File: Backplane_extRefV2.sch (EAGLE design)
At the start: 13 parts, among them J1 TFM-125-02-XXX-D-WT, U1 TLE2426CD

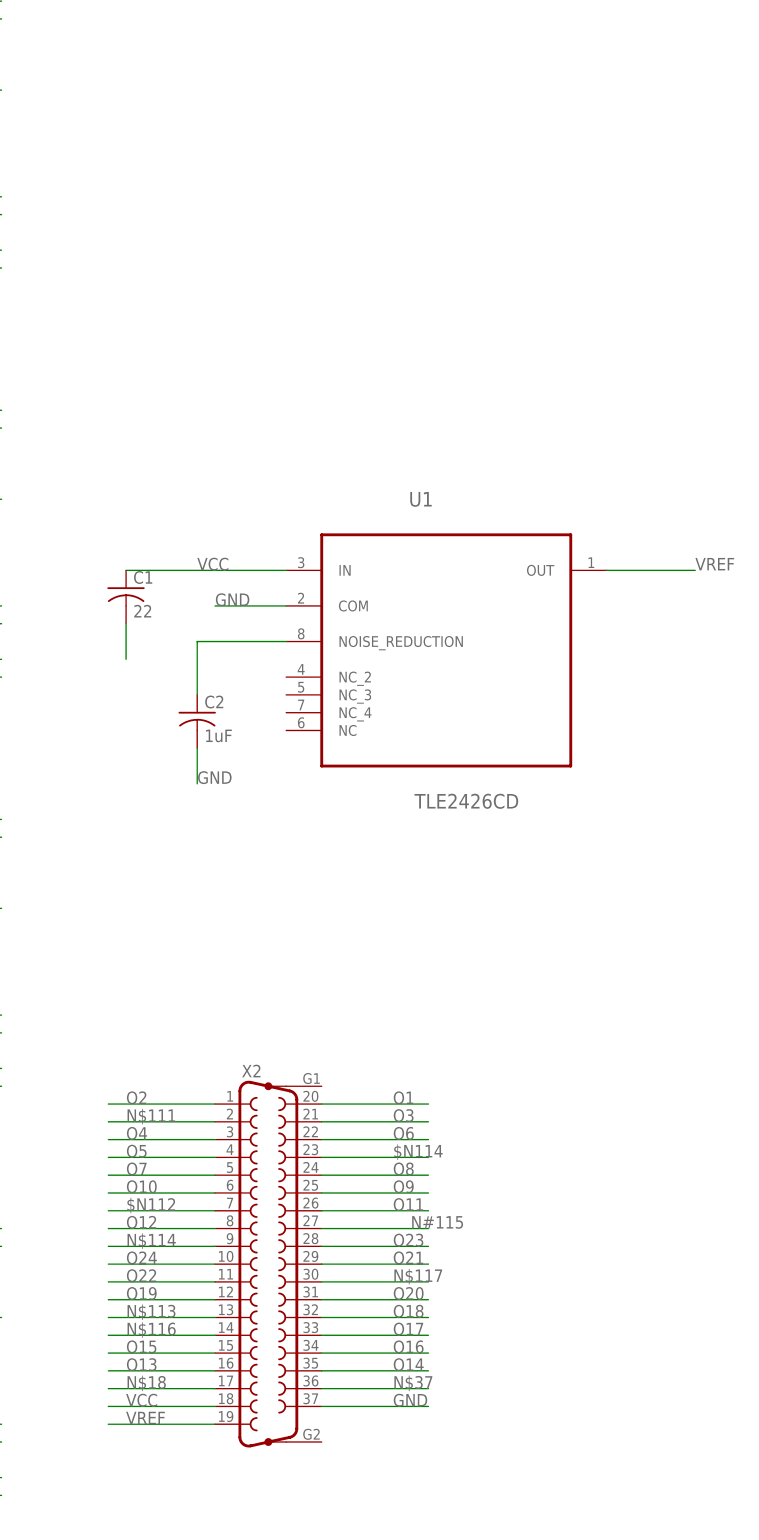
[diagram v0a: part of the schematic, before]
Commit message: minor updates to routing. Added DC-DC voltage converter/isolator to backplaneV2 & 24ch brd
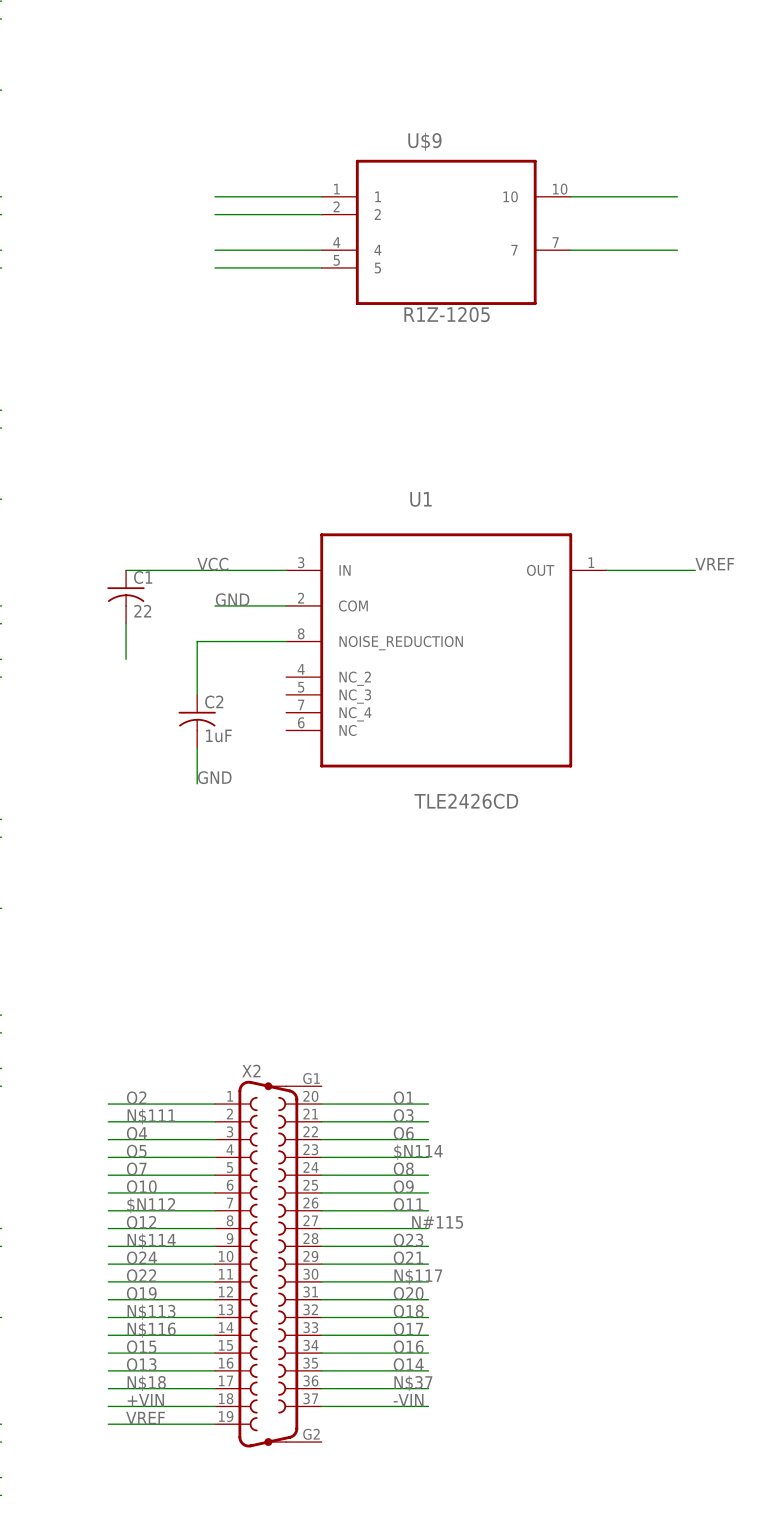
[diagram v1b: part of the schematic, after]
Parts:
- added U$9: R1Z-1205, tuckerLib:R1Z-1205
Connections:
- new net +VIN: U$9.2, X2.18
- new net -VIN: U$9.1, X2.37
- new net NC2: U$9.10
- net GND: now also U$9.4, U$9.5; no longer X2.37
- net VCC: now also U$9.7; no longer X2.18
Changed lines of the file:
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@@
 <part name="U$7" library="SAMTEC-FLE-Mxx-Sxx_By_element14_Batch_1" deviceset="FLE-116-01-G-DV" device=""/>
 <part name="U$8" library="SAMTEC-FLE-Mxx-Sxx_By_element14_Batch_1" deviceset="FLE-116-01-G-DV" device=""/>
+<part name="U$9" library="tuckerLib" deviceset="R1Z-1205" device=""/>
 </parts>
 <sheets>
@@
 <instance part="U$7" gate="A" x="66.04" y="-33.02"/>
 <instance part="U$8" gate="A" x="66.04" y="-93.98"/>
+<instance part="U$9" gate="G$1" x="162.56" y="182.88"/>
 </instances>
 <busses>
@@
 </segment>
 <segment>
-<pinref part="X2" gate="G$1" pin="37"/>
-<wire x1="144.78" y1="15.24" x2="160.02" y2="15.24" width="0.1524" layer="91"/>
-<label x="154.94" y="15.24" size="1.778" layer="95"/>
+<pinref part="U$9" gate="G$1" pin="4"/>
+<wire x1="144.78" y1="180.34" x2="129.54" y2="180.34" width="0.1524" layer="91"/>
+</segment>
+<segment>
+<pinref part="U$9" gate="G$1" pin="5"/>
+<wire x1="144.78" y1="177.8" x2="129.54" y2="177.8" width="0.1524" layer="91"/>
 </segment>
 </net>
@@
 </segment>
 <segment>
-<pinref part="X2" gate="G$1" pin="18"/>
-<wire x1="129.54" y1="15.24" x2="114.3" y2="15.24" width="0.1524" layer="91"/>
-<label x="116.84" y="15.24" size="1.778" layer="95"/>
+<pinref part="U$9" gate="G$1" pin="7"/>
+<wire x1="180.34" y1="180.34" x2="195.58" y2="180.34" width="0.1524" layer="91"/>
 </segment>
 </net>
@@
 </segment>
 </net>
+<net name="NC2" class="0">
+<segment>
+<pinref part="U$9" gate="G$1" pin="10"/>
+<wire x1="180.34" y1="187.96" x2="195.58" y2="187.96" width="0.1524" layer="91"/>
+</segment>
+</net>
+<net name="-VIN" class="0">
+<segment>
+<pinref part="U$9" gate="G$1" pin="1"/>
+<wire x1="144.78" y1="187.96" x2="129.54" y2="187.96" width="0.1524" layer="91"/>
+</segment>
+<segment>
+<pinref part="X2" gate="G$1" pin="37"/>
+<wire x1="144.78" y1="15.24" x2="160.02" y2="15.24" width="0.1524" layer="91"/>
+<label x="154.94" y="15.24" size="1.778" layer="95"/>
+</segment>
+</net>
+<net name="+VIN" class="0">
+<segment>
+<pinref part="U$9" gate="G$1" pin="2"/>
+<wire x1="144.78" y1="185.42" x2="129.54" y2="185.42" width="0.1524" layer="91"/>
+</segment>
+<segment>
+<pinref part="X2" gate="G$1" pin="18"/>
+<wire x1="129.54" y1="15.24" x2="114.3" y2="15.24" width="0.1524" layer="91"/>
+<label x="116.84" y="15.24" size="1.778" layer="95"/>
+</segment>
+</net>
